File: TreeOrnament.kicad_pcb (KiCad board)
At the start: 2 copper layers, 80 x 105 mm, 25 parts, among them J1 USB_B_Micro

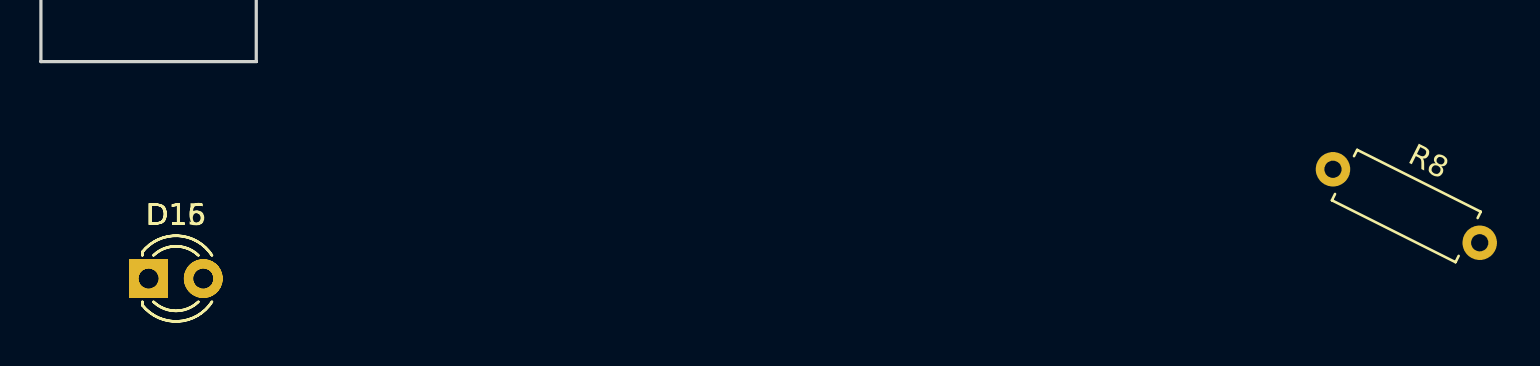
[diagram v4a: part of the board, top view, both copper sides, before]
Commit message: remove extra resistor and LEDs
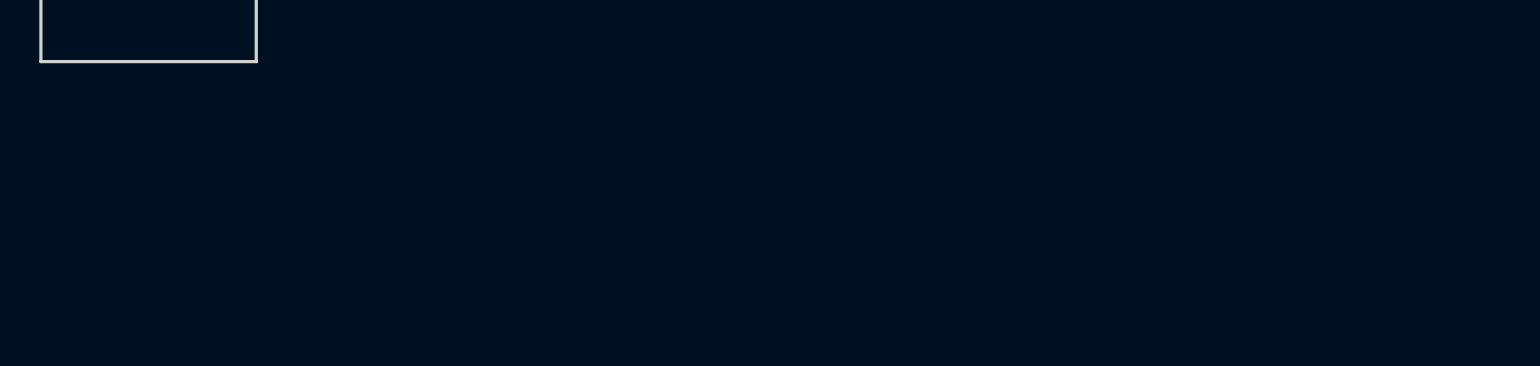
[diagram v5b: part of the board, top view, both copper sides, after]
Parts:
- removed D15, D16: LED, LEDs:LED_D3.0mm
- removed R8: 56, Resistors_THT:R_Axial_DIN0207_L6.3mm_D2.5mm_P7.62mm_Horizontal
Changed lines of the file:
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@@
 (kicad_pcb (version 4) (host pcbnew 4.0.7)
   (general
-    (links 34)
-    (no_connects 28)
+    (links 30)
+    (no_connects 30)
     (area 94.924999 29.924999 175.075001 135.075001)
     (thickness 1.6)
@@
     (tracks 0)
     (zones 0)
-    (modules 25)
-    (nets 22)
+    (modules 22)
+    (nets 20)
   )
   (page USLetter)
@@
   (net 18 "Net-(D13-Pad2)")
   (net 19 "Net-(D14-Pad2)")
-  (net 20 "Net-(D15-Pad2)")
-  (net 21 "Net-(D16-Pad2)")
   (net_class Default "This is the default net class."
     (clearance 0.2)
@@
     (add_net "Net-(D13-Pad2)")
     (add_net "Net-(D14-Pad2)")
-    (add_net "Net-(D15-Pad2)")
-    (add_net "Net-(D16-Pad2)")
     (add_net "Net-(D2-Pad2)")
     (add_net "Net-(D3-Pad2)")
@@
     )
   )
-  (module LEDs:LED_D3.0mm (layer F.Cu)
-    (at 135 145.075001)
-    (descr "LED, diameter 3.0mm, 2 pins")
-    (tags "LED diameter 3.0mm 2 pins")
-    (fp_text reference D15 (at 1.27 -2.96) (layer F.SilkS)
-      (effects (font (size 1 1) (thickness 0.15)))
-    )
-    (fp_text value LED (at 1.27 2.96) (layer F.Fab)
-      (effects (font (size 1 1) (thickness 0.15)))
-    )
-    (fp_arc (start 1.27 0) (end -0.23 -1.16619) (angle 284.3) (layer F.Fab) (width 0.1))
-    (fp_arc (start 1.27 0) (end -0.29 -1.235516) (angle 108.8) (layer F.SilkS) (width 0.12))
-    (fp_arc (start 1.27 0) (end -0.29 1.235516) (angle -108.8) (layer F.SilkS) (width 0.12))
-    (fp_arc (start 1.27 0) (end 0.229039 -1.08) (angle 87.9) (layer F.SilkS) (width 0.12))
-    (fp_arc (start 1.27 0) (end 0.229039 1.08) (angle -87.9) (layer F.SilkS) (width 0.12))
-    (fp_circle (center 1.27 0) (end 2.77 0) (layer F.Fab) (width 0.1))
-    (fp_line (start -0.23 -1.16619) (end -0.23 1.16619) (layer F.Fab) (width 0.1))
-    (fp_line (start -0.29 -1.236) (end -0.29 -1.08) (layer F.SilkS) (width 0.12))
-    (fp_line (start -0.29 1.08) (end -0.29 1.236) (layer F.SilkS) (width 0.12))
-    (fp_line (start -1.15 -2.25) (end -1.15 2.25) (layer F.CrtYd) (width 0.05))
-    (fp_line (start -1.15 2.25) (end 3.7 2.25) (layer F.CrtYd) (width 0.05))
-    (fp_line (start 3.7 2.25) (end 3.7 -2.25) (layer F.CrtYd) (width 0.05))
-    (fp_line (start 3.7 -2.25) (end -1.15 -2.25) (layer F.CrtYd) (width 0.05))
-    (pad 1 thru_hole rect (at 0 0) (size 1.8 1.8) (drill 0.9) (layers *.Cu *.Mask)
-      (net 1 GND))
-    (pad 2 thru_hole circle (at 2.54 0) (size 1.8 1.8) (drill 0.9) (layers *.Cu *.Mask)
-      (net 20 "Net-(D15-Pad2)"))
-    (model ${KISYS3DMOD}/LEDs.3dshapes/LED_D3.0mm.wrl
-      (at (xyz 0 0 0))
-      (scale (xyz 0.393701 0.393701 0.393701))
-      (rotate (xyz 0 0 0))
-    )
-  )
-  (module LEDs:LED_D3.0mm (layer F.Cu)
-    (at 135 145.075001)
-    (descr "LED, diameter 3.0mm, 2 pins")
-    (tags "LED diameter 3.0mm 2 pins")
-    (fp_text reference D16 (at 1.27 -2.96) (layer F.SilkS)
-      (effects (font (size 1 1) (thickness 0.15)))
-    )
-    (fp_text value LED (at 1.27 2.96) (layer F.Fab)
-      (effects (font (size 1 1) (thickness 0.15)))
-    )
-    (fp_arc (start 1.27 0) (end -0.23 -1.16619) (angle 284.3) (layer F.Fab) (width 0.1))
-    (fp_arc (start 1.27 0) (end -0.29 -1.235516) (angle 108.8) (layer F.SilkS) (width 0.12))
-    (fp_arc (start 1.27 0) (end -0.29 1.235516) (angle -108.8) (layer F.SilkS) (width 0.12))
-    (fp_arc (start 1.27 0) (end 0.229039 -1.08) (angle 87.9) (layer F.SilkS) (width 0.12))
-    (fp_arc (start 1.27 0) (end 0.229039 1.08) (angle -87.9) (layer F.SilkS) (width 0.12))
-    (fp_circle (center 1.27 0) (end 2.77 0) (layer F.Fab) (width 0.1))
-    (fp_line (start -0.23 -1.16619) (end -0.23 1.16619) (layer F.Fab) (width 0.1))
-    (fp_line (start -0.29 -1.236) (end -0.29 -1.08) (layer F.SilkS) (width 0.12))
-    (fp_line (start -0.29 1.08) (end -0.29 1.236) (layer F.SilkS) (width 0.12))
-    (fp_line (start -1.15 -2.25) (end -1.15 2.25) (layer F.CrtYd) (width 0.05))
-    (fp_line (start -1.15 2.25) (end 3.7 2.25) (layer F.CrtYd) (width 0.05))
-    (fp_line (start 3.7 2.25) (end 3.7 -2.25) (layer F.CrtYd) (width 0.05))
-    (fp_line (start 3.7 -2.25) (end -1.15 -2.25) (layer F.CrtYd) (width 0.05))
-    (pad 1 thru_hole rect (at 0 0) (size 1.8 1.8) (drill 0.9) (layers *.Cu *.Mask)
-      (net 20 "Net-(D15-Pad2)"))
-    (pad 2 thru_hole circle (at 2.54 0) (size 1.8 1.8) (drill 0.9) (layers *.Cu *.Mask)
-      (net 21 "Net-(D16-Pad2)"))
-    (model ${KISYS3DMOD}/LEDs.3dshapes/LED_D3.0mm.wrl
-      (at (xyz 0 0 0))
-      (scale (xyz 0.393701 0.393701 0.393701))
-      (rotate (xyz 0 0 0))
-    )
-  )
   (module Resistors_THT:R_Axial_DIN0207_L6.3mm_D2.5mm_P7.62mm_Horizontal (layer F.Cu)
     (at 125 65 333.4)
@@
     (model ${KISYS3DMOD}/Resistors_THT.3dshapes/R_Axial_DIN0207_L6.3mm_D2.5mm_P7.62mm_Horizontal.wrl
       (at (xyz 0 0 0))
-      (scale (xyz 0.393701 0.393701 0.393701))
-      (rotate (xyz 0 0 0))
-    )
-  )
-  (module Resistors_THT:R_Axial_DIN0207_L6.3mm_D2.5mm_P7.62mm_Horizontal (layer F.Cu)
-    (at 190 140 333.4)
-    (descr "Resistor, Axial_DIN0207 series, Axial, Horizontal, pin pitch=7.62mm, 0.25W = 1/4W, length*diameter=6.3*2.5mm^2, http://cdn-reichelt.de/documents/datenblatt/B400/1_4W%23YAG.pdf")
-    (tags "Resistor Axial_DIN0207 series Axial Horizontal pin pitch 7.62mm 0.25W = 1/4W length 6.3mm diameter 2.5mm")
-    (fp_text reference R8 (at 3.81 -2.31 333.4) (layer F.SilkS)
-      (effects (font (size 1 1) (thickness 0.15)))
-    )
-    (fp_text value 56 (at 3.81 2.31 333.4) (layer F.Fab)
-      (effects (font (size 1 1) (thickness 0.15)))
-    )
-    (fp_line (start 0.66 -1.25) (end 0.66 1.25) (layer F.Fab) (width 0.1))
-    (fp_line (start 0.66 1.25) (end 6.96 1.25) (layer F.Fab) (width 0.1))
-    (fp_line (start 6.96 1.25) (end 6.96 -1.25) (layer F.Fab) (width 0.1))
-    (fp_line (start 6.96 -1.25) (end 0.66 -1.25) (layer F.Fab) (width 0.1))
-    (fp_line (start 0 0) (end 0.66 0) (layer F.Fab) (width 0.1))
-    (fp_line (start 7.62 0) (end 6.96 0) (layer F.Fab) (width 0.1))
-    (fp_line (start 0.6 -0.98) (end 0.6 -1.31) (layer F.SilkS) (width 0.12))
-    (fp_line (start 0.6 -1.31) (end 7.02 -1.31) (layer F.SilkS) (width 0.12))
-    (fp_line (start 7.02 -1.31) (end 7.02 -0.98) (layer F.SilkS) (width 0.12))
-    (fp_line (start 0.6 0.98) (end 0.6 1.31) (layer F.SilkS) (width 0.12))
-    (fp_line (start 0.6 1.31) (end 7.02 1.31) (layer F.SilkS) (width 0.12))
-    (fp_line (start 7.02 1.31) (end 7.02 0.98) (layer F.SilkS) (width 0.12))
-    (fp_line (start -1.05 -1.6) (end -1.05 1.6) (layer F.CrtYd) (width 0.05))
-    (fp_line (start -1.05 1.6) (end 8.7 1.6) (layer F.CrtYd) (width 0.05))
-    (fp_line (start 8.7 1.6) (end 8.7 -1.6) (layer F.CrtYd) (width 0.05))
-    (fp_line (start 8.7 -1.6) (end -1.05 -1.6) (layer F.CrtYd) (width 0.05))
-    (pad 1 thru_hole circle (at 0 0 333.4) (size 1.6 1.6) (drill 0.8) (layers *.Cu *.Mask)
-      (net 10 +5V))
-    (pad 2 thru_hole oval (at 7.62 0 333.4) (size 1.6 1.6) (drill 0.8) (layers *.Cu *.Mask)
-      (net 21 "Net-(D16-Pad2)"))
-    (model ${KISYS3DMOD}/Resistors_THT.3dshapes/R_Axial_DIN0207_L6.3mm_D2.5mm_P7.62mm_Horizontal.wrl
-      (at (xyz 0 0 0))

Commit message: Add candy canes and ornaments to tree.
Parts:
- added REF**: CandyCane, myLibrary:CandyCane, F.Cu at (144.0, 55.0)
- added REF**: Ornament, myLibrary:Ornament, F.Cu at (136.0, 59.0)
- added REF**: Ornament, myLibrary:Ornament, F.Cu at (137.0, 41.0)
- added REF**: Ornament, myLibrary:Ornament, F.Cu at (124.0, 52.0)
- added REF**: CandyCane, myLibrary:CandyCane, F.Cu at (123.0, 74.0)
- added REF**: CandyCane, myLibrary:CandyCane, F.Cu at (116.0, 114.0)
- added REF**: CandyCane, myLibrary:CandyCane, F.Cu at (151.0, 87.0)
- added REF**: Ornament, myLibrary:Ornament, F.Cu at (134.0, 115.0)
- added REF**: Ornament, myLibrary:Ornament, F.Cu at (106.0, 115.0)
- added REF**: Ornament, myLibrary:Ornament, F.Cu at (118.0, 86.0)
- added REF**: Ornament, myLibrary:Ornament, F.Cu at (147.0, 104.0)
- added REF**: Ornament, myLibrary:Ornament, F.Cu at (137.0, 80.0)
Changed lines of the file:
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@@
 (kicad_pcb (version 4) (host pcbnew 4.0.7)
   (general
-    (links 30)
+    (links 0)
     (no_connects 30)
     (area 94.924999 29.924999 175.075001 135.075001)
@@
     (tracks 0)
     (zones 0)
-    (modules 22)
+    (modules 34)
     (nets 20)
   )
@@
     (add_net "Net-(J1-Pad4)")
   )
+  (module myLibrary:CandyCane (layer F.Cu)
+    (at 144 55 340)
+    (fp_text reference REF** (at 0 -4.5 340) (layer F.SilkS) hide
+      (effects (font (size 1 1) (thickness 0.15)))
+    )
+    (fp_text value CandyCane (at 0 2.5 340) (layer F.Fab) hide
+      (effects (font (size 1 1) (thickness 0.15)))
+    )
+    (fp_line (start 1 -2.5) (end 1 1.5) (layer F.SilkS) (width 0.5))
+    (fp_arc (start 0 -2.5) (end -1 -2.5) (angle 180) (layer F.SilkS) (width 0.5))
+  )
+  (module myLibrary:CandyCane (layer F.Cu)
+    (at 123 74 340)
+    (fp_text reference REF** (at 0 -4.5 340) (layer F.SilkS) hide
+      (effects (font (size 1 1) (thickness 0.15)))
+    )
+    (fp_text value CandyCane (at 0 2.5 340) (layer F.Fab) hide
+      (effects (font (size 1 1) (thickness 0.15)))
+    )
+    (fp_line (start 1 -2.5) (end 1 1.5) (layer F.SilkS) (width 0.5))
+    (fp_arc (start 0 -2.5) (end -1 -2.5) (angle 180) (layer F.SilkS) (width 0.5))
+  )
+  (module myLibrary:CandyCane (layer F.Cu)
+    (at 116 114 340)
+    (fp_text reference REF** (at 0 -4.5 340) (layer F.SilkS) hide
+      (effects (font (size 1 1) (thickness 0.15)))
+    )
+    (fp_text value CandyCane (at 0 2.5 340) (layer F.Fab) hide
+      (effects (font (size 1 1) (thickness 0.15)))
+    )
+    (fp_line (start 1 -2.5) (end 1 1.5) (layer F.SilkS) (width 0.5))
+    (fp_arc (start 0 -2.5) (end -1 -2.5) (angle 180) (layer F.SilkS) (width 0.5))
+  )
   (module LEDs:LED_D3.0mm (layer F.Cu)
     (at 111 106)
@@
     )
   )
+  (module myLibrary:CandyCane (layer F.Cu)
+    (at 151 87 340)
+    (fp_text reference REF** (at 0 -4.5 340) (layer F.SilkS) hide
+      (effects (font (size 1 1) (thickness 0.15)))
+    )
+    (fp_text value CandyCane (at 0 2.5 340) (layer F.Fab) hide
+      (effects (font (size 1 1) (thickness 0.15)))
+    )
+    (fp_line (start 1 -2.5) (end 1 1.5) (layer F.SilkS) (width 0.5))
+    (fp_arc (start 0 -2.5) (end -1 -2.5) (angle 180) (layer F.SilkS) (width 0.5))
+  )
+  (module myLibrary:Ornament (layer F.Cu)
+    (at 134 115)
+    (fp_text reference REF** (at 0 -3.5) (layer F.SilkS) hide
+      (effects (font (size 1 1) (thickness 0.15)))
+    )
+    (fp_text value Ornament (at 0 2.5) (layer F.Fab) hide
+      (effects (font (size 1 1) (thickness 0.15)))
+    )
+    (pad 1 smd circle (at 0 0) (size 4 4) (layers F.Cu F.Mask))
+    (pad 2 smd rect (at 0 -2) (size 1 1) (layers F.Cu F.Mask))
+    (pad 3 smd circle (at 0 -2.5) (size 0.5 0.5) (layers F.Cu F.Mask))
+  )
+  (module myLibrary:Ornament (layer F.Cu)
+    (at 106 115)
+    (fp_text reference REF** (at 0 -3.5) (layer F.SilkS) hide
+      (effects (font (size 1 1) (thickness 0.15)))
+    )
+    (fp_text value Ornament (at 0 2.5) (layer F.Fab) hide
+      (effects (font (size 1 1) (thickness 0.15)))
+    )
+    (pad 1 smd circle (at 0 0) (size 4 4) (layers F.Cu F.Mask))
+    (pad 2 smd rect (at 0 -2) (size 1 1) (layers F.Cu F.Mask))
+    (pad 3 smd circle (at 0 -2.5) (size 0.5 0.5) (layers F.Cu F.Mask))
+  )
+  (module myLibrary:Ornament (layer F.Cu)
+    (at 118 86)
+    (fp_text reference REF** (at 0 -3.5) (layer F.SilkS) hide
+      (effects (font (size 1 1) (thickness 0.15)))
+    )
+    (fp_text value Ornament (at 0 2.5) (layer F.Fab) hide
+      (effects (font (size 1 1) (thickness 0.15)))
+    )
+    (pad 1 smd circle (at 0 0) (size 4 4) (layers F.Cu F.Mask))
+    (pad 2 smd rect (at 0 -2) (size 1 1) (layers F.Cu F.Mask))
+    (pad 3 smd circle (at 0 -2.5) (size 0.5 0.5) (layers F.Cu F.Mask))
+  )
+  (module myLibrary:Ornament (layer F.Cu)
+    (at 147 104)
+    (fp_text reference REF** (at 0 -3.5) (layer F.SilkS) hide
+      (effects (font (size 1 1) (thickness 0.15)))
+    )
+    (fp_text value Ornament (at 0 2.5) (layer F.Fab) hide
+      (effects (font (size 1 1) (thickness 0.15)))
+    )
+    (pad 1 smd circle (at 0 0) (size 4 4) (layers F.Cu F.Mask))
+    (pad 2 smd rect (at 0 -2) (size 1 1) (layers F.Cu F.Mask))
+    (pad 3 smd circle (at 0 -2.5) (size 0.5 0.5) (layers F.Cu F.Mask))
+  )
+  (module myLibrary:Ornament (layer F.Cu)
+    (at 137 80)
+    (fp_text reference REF** (at 0 -3.5) (layer F.SilkS) hide
+      (effects (font (size 1 1) (thickness 0.15)))
+    )
+    (fp_text value Ornament (at 0 2.5) (layer F.Fab) hide
+      (effects (font (size 1 1) (thickness 0.15)))
+    )
+    (pad 1 smd circle (at 0 0) (size 4 4) (layers F.Cu F.Mask))
+    (pad 2 smd rect (at 0 -2) (size 1 1) (layers F.Cu F.Mask))
+    (pad 3 smd circle (at 0 -2.5) (size 0.5 0.5) (layers F.Cu F.Mask))
+  )
+  (module myLibrary:Ornament (layer F.Cu)
+    (at 136 59)
+    (fp_text reference REF** (at 0 -3.5) (layer F.SilkS) hide
+      (effects (font (size 1 1) (thickness 0.15)))
+    )
+    (fp_text value Ornament (at 0 2.5) (layer F.Fab) hide
+      (effects (font (size 1 1) (thickness 0.15)))
+    )
+    (pad 1 smd circle (at 0 0) (size 4 4) (layers F.Cu F.Mask))
+    (pad 2 smd rect (at 0 -2) (size 1 1) (layers F.Cu F.Mask))
+    (pad 3 smd circle (at 0 -2.5) (size 0.5 0.5) (layers F.Cu F.Mask))
+  )
+  (module myLibrary:Ornament (layer F.Cu)
+    (at 137 41)
+    (fp_text reference REF** (at 0 -3.5) (layer F.SilkS) hide
+      (effects (font (size 1 1) (thickness 0.15)))
+    )
+    (fp_text value Ornament (at 0 2.5) (layer F.Fab) hide
+      (effects (font (size 1 1) (thickness 0.15)))
+    )
+    (pad 1 smd circle (at 0 0) (size 4 4) (layers F.Cu F.Mask))
+    (pad 2 smd rect (at 0 -2) (size 1 1) (layers F.Cu F.Mask))
+    (pad 3 smd circle (at 0 -2.5) (size 0.5 0.5) (layers F.Cu F.Mask))
+  )
+  (module myLibrary:Ornament (layer F.Cu)
+    (at 124 52)
+    (fp_text reference REF** (at 0 -3.5) (layer F.SilkS) hide
+      (effects (font (size 1 1) (thickness 0.15)))
+    )
+    (fp_text value Ornament (at 0 2.5) (layer F.Fab) hide
+      (effects (font (size 1 1) (thickness 0.15)))
+    )
+    (pad 1 smd circle (at 0 0) (size 4 4) (layers F.Cu F.Mask))
+    (pad 2 smd rect (at 0 -2) (size 1 1) (layers F.Cu F.Mask))
+    (pad 3 smd circle (at 0 -2.5) (size 0.5 0.5) (layers F.Cu F.Mask))
+  )
   (gr_line (start 95 120) (end 130 120) (angle 90) (layer Edge.Cuts) (width 0.15))

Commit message: expose bare FR4 for tree trunk
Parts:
- added REF**: Trunk, myLibrary:Trunk, F.Cu at (135.0, 127.5)
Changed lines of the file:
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@@
     (tracks 0)
     (zones 0)
-    (modules 34)
+    (modules 35)
     (nets 20)
   )
@@
     (pad 3 smd circle (at 0 -2.5) (size 0.5 0.5) (layers F.Cu F.Mask))
   )
+  (module myLibrary:Trunk (layer F.Cu)
+    (at 135 127.5)
+    (fp_text reference REF** (at 0 -8.5) (layer F.SilkS) hide
+      (effects (font (size 1 1) (thickness 0.15)))
+    )
+    (fp_text value Trunk (at 0 8.5) (layer F.Fab) hide
+      (effects (font (size 1 1) (thickness 0.15)))
+    )
+    (pad "" smd rect (at 0 0) (size 10 15) (layers F.Mask))
+  )
   (gr_line (start 95 120) (end 130 120) (angle 90) (layer Edge.Cuts) (width 0.15))

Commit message: Adjust garlands.
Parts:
- added REF**: CandyCane, myLibrary:CandyCane, F.Cu at (128.0, 99.0)
- moved R1 4.24 mm to (112.0, 98.0)
- moved R2 4.24 mm to (122.0, 103.0)
- moved R3 4.24 mm to (132.0, 108.0)
- moved R4 4.24 mm to (142.0, 113.0)
- moved D2 3.16 mm to (123.0, 113.0)
- moved R5 1.41 mm to (126.0, 64.0)
- moved R6 1.41 mm to (136.0, 69.0)
- moved R7 1.41 mm to (146.0, 74.0)
- moved REF** 1.41 mm to (133.0, 116.0)
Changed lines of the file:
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@@
     (tracks 0)
     (zones 0)
-    (modules 35)
+    (modules 36)
     (nets 20)
   )
@@
   )
   (module LEDs:LED_D3.0mm (layer F.Cu)
-    (at 124 110)
+    (at 123 113)
     (descr "LED, diameter 3.0mm, 2 pins")
     (tags "LED diameter 3.0mm 2 pins")
@@
   )
   (module Resistors_THT:R_Axial_DIN0207_L6.3mm_D2.5mm_P7.62mm_Horizontal (layer F.Cu)
-    (at 115 95 333.4)
+    (at 112 98 333.4)
     (descr "Resistor, Axial_DIN0207 series, Axial, Horizontal, pin pitch=7.62mm, 0.25W = 1/4W, length*diameter=6.3*2.5mm^2, http://cdn-reichelt.de/documents/datenblatt/B400/1_4W%23YAG.pdf")
     (tags "Resistor Axial_DIN0207 series Axial Horizontal pin pitch 7.62mm 0.25W = 1/4W length 6.3mm diameter 2.5mm")
@@
   )
   (module Resistors_THT:R_Axial_DIN0207_L6.3mm_D2.5mm_P7.62mm_Horizontal (layer F.Cu)
-    (at 125 100 333.4)
+    (at 122 103 333.4)
     (descr "Resistor, Axial_DIN0207 series, Axial, Horizontal, pin pitch=7.62mm, 0.25W = 1/4W, length*diameter=6.3*2.5mm^2, http://cdn-reichelt.de/documents/datenblatt/B400/1_4W%23YAG.pdf")
     (tags "Resistor Axial_DIN0207 series Axial Horizontal pin pitch 7.62mm 0.25W = 1/4W length 6.3mm diameter 2.5mm")
@@
   )
   (module Resistors_THT:R_Axial_DIN0207_L6.3mm_D2.5mm_P7.62mm_Horizontal (layer F.Cu)
-    (at 135 105 333.4)
+    (at 132 108 333.4)
     (descr "Resistor, Axial_DIN0207 series, Axial, Horizontal, pin pitch=7.62mm, 0.25W = 1/4W, length*diameter=6.3*2.5mm^2, http://cdn-reichelt.de/documents/datenblatt/B400/1_4W%23YAG.pdf")
     (tags "Resistor Axial_DIN0207 series Axial Horizontal pin pitch 7.62mm 0.25W = 1/4W length 6.3mm diameter 2.5mm")
@@
   )
   (module Resistors_THT:R_Axial_DIN0207_L6.3mm_D2.5mm_P7.62mm_Horizontal (layer F.Cu)
-    (at 145 110 333.4)
+    (at 142 113 333.4)
     (descr "Resistor, Axial_DIN0207 series, Axial, Horizontal, pin pitch=7.62mm, 0.25W = 1/4W, length*diameter=6.3*2.5mm^2, http://cdn-reichelt.de/documents/datenblatt/B400/1_4W%23YAG.pdf")
     (tags "Resistor Axial_DIN0207 series Axial Horizontal pin pitch 7.62mm 0.25W = 1/4W length 6.3mm diameter 2.5mm")
@@
   )
   (module Resistors_THT:R_Axial_DIN0207_L6.3mm_D2.5mm_P7.62mm_Horizontal (layer F.Cu)
-    (at 125 65 333.4)
+    (at 126 64 333.4)
     (descr "Resistor, Axial_DIN0207 series, Axial, Horizontal, pin pitch=7.62mm, 0.25W = 1/4W, length*diameter=6.3*2.5mm^2, http://cdn-reichelt.de/documents/datenblatt/B400/1_4W%23YAG.pdf")
     (tags "Resistor Axial_DIN0207 series Axial Horizontal pin pitch 7.62mm 0.25W = 1/4W length 6.3mm diameter 2.5mm")
@@
   )
   (module Resistors_THT:R_Axial_DIN0207_L6.3mm_D2.5mm_P7.62mm_Horizontal (layer F.Cu)
-    (at 135 70 333.4)
+    (at 136 69 333.4)
     (descr "Resistor, Axial_DIN0207 series, Axial, Horizontal, pin pitch=7.62mm, 0.25W = 1/4W, length*diameter=6.3*2.5mm^2, http://cdn-reichelt.de/documents/datenblatt/B400/1_4W%23YAG.pdf")
     (tags "Resistor Axial_DIN0207 series Axial Horizontal pin pitch 7.62mm 0.25W = 1/4W length 6.3mm diameter 2.5mm")
@@
   )
   (module Resistors_THT:R_Axial_DIN0207_L6.3mm_D2.5mm_P7.62mm_Horizontal (layer F.Cu)
-    (at 145 75 333.4)
+    (at 146 74 333.4)
     (descr "Resistor, Axial_DIN0207 series, Axial, Horizontal, pin pitch=7.62mm, 0.25W = 1/4W, length*diameter=6.3*2.5mm^2, http://cdn-reichelt.de/documents/datenblatt/B400/1_4W%23YAG.pdf")
     (tags "Resistor Axial_DIN0207 series Axial Horizontal pin pitch 7.62mm 0.25W = 1/4W length 6.3mm diameter 2.5mm")
@@
   )
   (module myLibrary:Ornament (layer F.Cu)
-    (at 134 115)
+    (at 133 116)
     (fp_text reference REF** (at 0 -3.5) (layer F.SilkS) hide
       (effects (font (size 1 1) (thickness 0.15)))
@@
     (pad "" smd rect (at 0 0) (size 10 15) (layers F.Mask))
   )
+  (module myLibrary:CandyCane (layer F.Cu)
+    (at 128 99 340)
+    (fp_text reference REF** (at 0 -4.5 340) (layer F.SilkS) hide
+      (effects (font (size 1 1) (thickness 0.15)))
+    )
+    (fp_text value CandyCane (at 0 2.5 340) (layer F.Fab) hide
+      (effects (font (size 1 1) (thickness 0.15)))
+    )
+    (fp_line (start 1 -2.5) (end 1 1.5) (layer F.SilkS) (width 0.5))
+    (fp_arc (start 0 -2.5) (end -1 -2.5) (angle 180) (layer F.SilkS) (width 0.5))
+  )
   (gr_line (start 95 120) (end 130 120) (angle 90) (layer Edge.Cuts) (width 0.15))
